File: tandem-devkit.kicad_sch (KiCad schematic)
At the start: 24 parts, among them J101 Conn_01x03, J102 Conn_01x03, J103 Conn_01x04, J104 Conn_01x02, J105 QWIIC I2C Connector

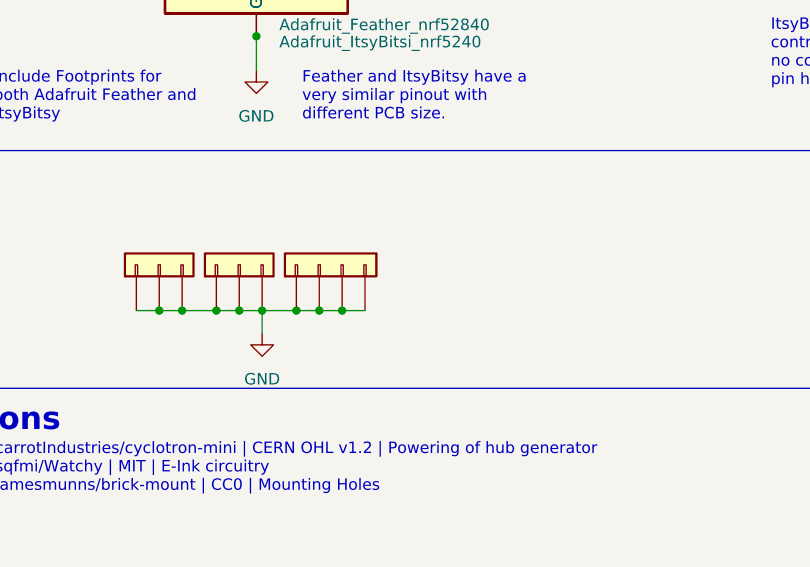
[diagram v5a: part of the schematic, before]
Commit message: prepare for touch button routing
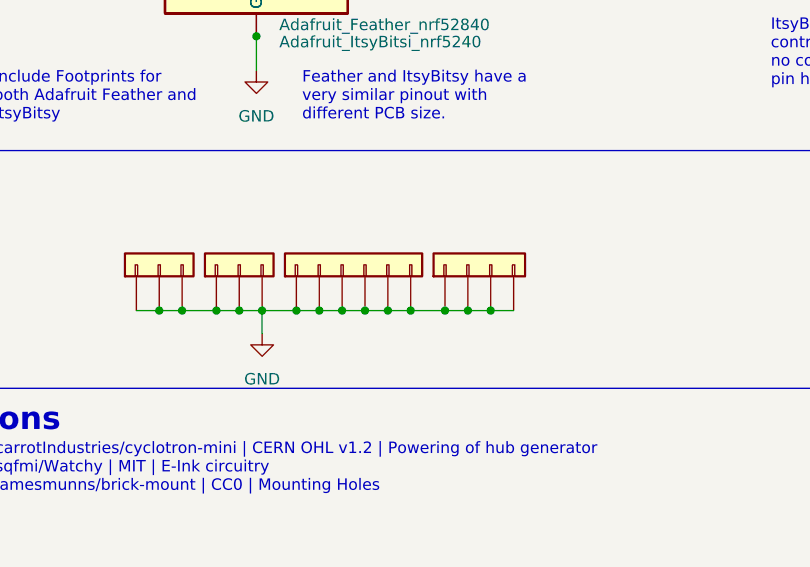
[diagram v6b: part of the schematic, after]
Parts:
- added J?: Conn_01x04, project-lib:brick-2x2, symbol Connector_Generic:Conn_01x04
- J103: value Conn_01x04 -> Conn_01x06; footprint brick-mount:brick-1x4 -> brick-mount:brick-1x6; symbol Connector_Generic:Conn_01x04 -> Connector_Generic:Conn_01x06
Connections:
- net GND: now also J103.5 (Pin_5), J103.6 (Pin_6), J?.1 (Pin_1), J?.2 (Pin_2), J?.3 (Pin_3), J?.4 (Pin_4)
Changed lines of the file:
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@@
   (junction (at 207.645 138.43) (diameter 0) (color 0 0 0 0)
   )
+  (junction (at 73.025 157.48) (diameter 0) (color 0 0 0 0)
+  )
   (junction (at 73.66 96.52) (diameter 0) (color 0 0 0 0)
   )
   (junction (at 48.26 83.82) (diameter 0) (color 0 0 0 0)
   )
+  (junction (at 86.995 157.48) (diameter 0) (color 0 0 0 0)
+  )
   (junction (at 48.26 73.66) (diameter 0) (color 0 0 0 0)
   )
@@
   (junction (at 63.5 63.5) (diameter 0) (color 0 0 0 0)
   )
+  (junction (at 75.565 157.48) (diameter 0) (color 0 0 0 0)
+  )
   (junction (at 61.595 157.48) (diameter 0) (color 0 0 0 0)
   )
   (junction (at 48.26 99.06) (diameter 0) (color 0 0 0 0)
   )
+  (junction (at 84.455 157.48) (diameter 0) (color 0 0 0 0)
+  )
   (junction (at 60.96 127) (diameter 0) (color 0 0 0 0)
   )
@@
   (junction (at 56.515 157.48) (diameter 0) (color 0 0 0 0)
   )
+  (junction (at 78.105 157.48) (diameter 0) (color 0 0 0 0)
+  )
   (junction (at 70.485 157.48) (diameter 0) (color 0 0 0 0)
   )
@@
   )
   (junction (at 48.26 88.9) (diameter 0) (color 0 0 0 0)
+  )
+  (junction (at 81.915 157.48) (diameter 0) (color 0 0 0 0)
   )
   (junction (at 48.26 106.68) (diameter 0) (color 0 0 0 0)
@@
     (stroke (width 0) (type default) (color 0 0 0 0))
   )
+  (wire (pts (xy 86.995 157.48) (xy 89.535 157.48))
+    (stroke (width 0) (type default) (color 0 0 0 0))
+  )
   (polyline (pts (xy 163.195 139.7) (xy 163.195 35.56))
     (stroke (width 0) (type default) (color 0 0 0 0))
@@
     (stroke (width 0) (type default) (color 0 0 0 0))
   )
+  (wire (pts (xy 78.105 157.48) (xy 81.915 157.48))
+    (stroke (width 0) (type default) (color 0 0 0 0))
+  )
   (wire (pts (xy 60.96 127) (xy 60.96 130.81))
     (stroke (width 0) (type default) (color 0 0 0 0))
@@
   )
   (wire (pts (xy 56.515 157.48) (xy 59.055 157.48))
+    (stroke (width 0) (type default) (color 0 0 0 0))
+  )
+  (wire (pts (xy 75.565 157.48) (xy 78.105 157.48))
     (stroke (width 0) (type default) (color 0 0 0 0))
   )
@@
     (stroke (width 0) (type default) (color 0 0 0 0))
   )
+  (wire (pts (xy 81.915 157.48) (xy 84.455 157.48))
+    (stroke (width 0) (type default) (color 0 0 0 0))
+  )
   (polyline (pts (xy 174.244 166.116) (xy 174.244 195.58))
     (stroke (width 0) (type solid) (color 221 0 0 1))
@@
     (stroke (width 0) (type solid) (color 221 0 0 1))
   )
+  (wire (pts (xy 84.455 157.48) (xy 86.995 157.48))
+    (stroke (width 0) (type default) (color 0 0 0 0))
+  )
   (wire (pts (xy 43.815 114.3) (xy 48.26 114.3))
     (stroke (width 0) (type default) (color 0 0 0 0))
@@
   )
   (wire (pts (xy 47.625 157.48) (xy 50.165 157.48))
+    (stroke (width 0) (type default) (color 0 0 0 0))
+  )
+  (wire (pts (xy 73.025 157.48) (xy 75.565 157.48))
     (stroke (width 0) (type default) (color 0 0 0 0))
   )
@@
     (pin "3")
   )
+  (symbol (lib_id "Connector_Generic:Conn_01x04") (at 84.455 152.4 90) (unit 1)
+    (in_bom yes) (on_board yes) (fields_autoplaced)
+    (property "Reference" "J?" (id 0) (at 85.725 146.05 90)
+      (effects (font (size 1.27 1.27)) hide)
+    )
+    (property "Value" "Conn_01x04" (id 1) (at 85.725 148.59 90)
+      (effects (font (size 1.27 1.27)) hide)
+    )
+    (property "Footprint" "project-lib:brick-2x2" (id 2) (at 84.455 152.4 0)
+      (effects (font (size 1.27 1.27)) hide)
+    )
+    (property "Datasheet" "~" (id 3) (at 84.455 152.4 0)
+      (effects (font (size 1.27 1.27)) hide)
+    )
+    (pin "1")
+    (pin "2")
+    (pin "3")
+    (pin "4")
+  )
   (symbol (lib_id "Device:R") (at 198.12 110.49 0) (unit 1)
     (in_bom yes) (on_board yes)
@@
     (pin "2")
   )
-  (symbol (lib_id "Connector_Generic:Conn_01x04") (at 67.945 152.4 90) (unit 1)
+  (symbol (lib_id "Connector_Generic:Conn_01x06") (at 70.485 152.4 90) (unit 1)
     (in_bom yes) (on_board yes) (fields_autoplaced)
-    (property "Reference" "J103" (id 0) (at 73.66 151.1299 90)
+    (property "Reference" "J103" (id 0) (at 76.2 151.1299 90)
       (effects (font (size 1.27 1.27)) (justify right) hide)
     )
-    (property "Value" "Conn_01x04" (id 1) (at 73.66 153.6699 90)
+    (property "Value" "Conn_01x06" (id 1) (at 76.2 153.6699 90)
       (effects (font (size 1.27 1.27)) (justify right) hide)
     )
-    (property "Footprint" "brick-mount:brick-1x4" (id 2) (at 67.945 152.4 0)
-      (effects (font (size 1.27 1.27)) hide)
-    )
-    (property "Datasheet" "~" (id 3) (at 67.945 152.4 0)
+    (property "Footprint" "brick-mount:brick-1x6" (id 2) (at 70.485 152.4 0)
+      (effects (font (size 1.27 1.27)) hide)
+    )
+    (property "Datasheet" "~" (id 3) (at 70.485 152.4 0)
       (effects (font (size 1.27 1.27)) hide)
     )
@@
     (pin "3")
     (pin "4")
+    (pin "5")
+    (pin "6")
   )
   (symbol (lib_id "Device:R") (at 40.005 86.36 90) (unit 1)
@@
     )
     (path "/e95b30be-c55c-4c78-9932-8a6370cf2f1d"
-      (reference "J103") (unit 1) (value "Conn_01x04") (footprint "brick-mount:brick-1x4")
+      (reference "J103") (unit 1) (value "Conn_01x06") (footprint "brick-mount:brick-1x6")
     )
     (path "/ec9c36e9-9c09-4abd-9e21-b989c784b09b"
@@
       (reference "J303") (unit 1) (value "FPC10(0.5MM)") (footprint "project-lib:jlcpcb-C11050_FFC_1x10-1MP_P0.50mm_Horizontal")
     )
+    (path "/d65d0648-9caf-48a8-a5f7-2e07080e3aea"
+      (reference "J?") (unit 1) (value "Conn_01x04") (footprint "project-lib:brick-2x2")
+    )
     (path "/d5fdcc1b-217f-4399-86f5-956578dadb93/7c178f84-7da2-4e79-b146-9dc5d286d2ba"

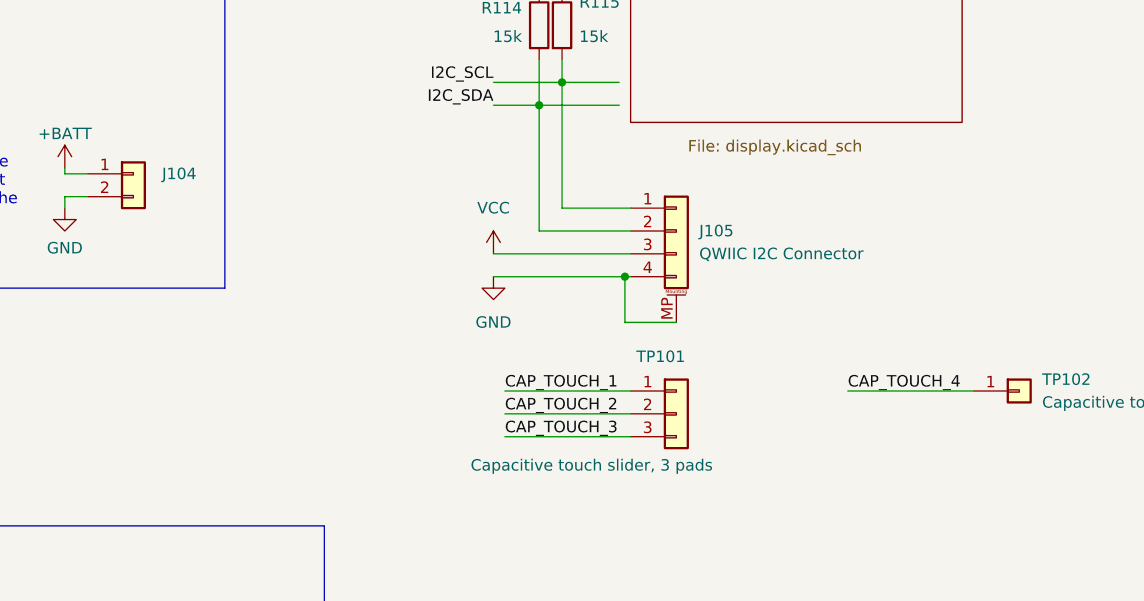
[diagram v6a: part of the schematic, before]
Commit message: PCB: route cap buttons and adjust zones
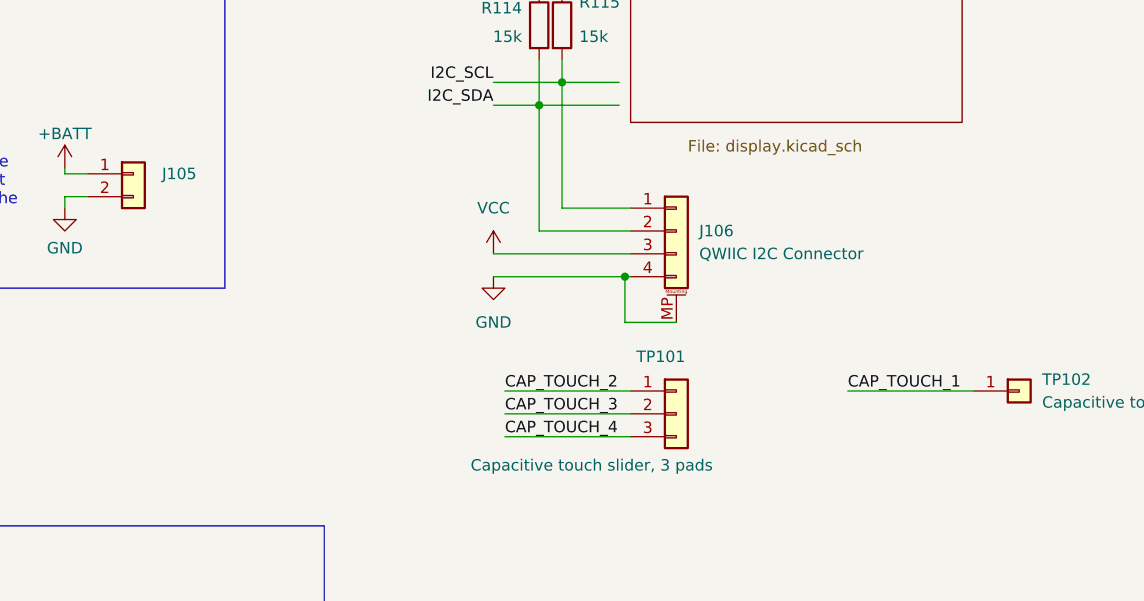
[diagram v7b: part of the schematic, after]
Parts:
- gave numbers to parts that had none: 1
- renumbered J104 to J105, J105 to J106
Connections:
- net CAP_TOUCH_1: now also TP102.1 (Pin_1); no longer TP101.1 (Pin_1)
- net CAP_TOUCH_2: now also TP101.1 (Pin_1); no longer TP101.2 (Pin_2)
- net CAP_TOUCH_3: now also TP101.2 (Pin_2); no longer TP101.3 (Pin_3)
- net CAP_TOUCH_4: now also TP101.3 (Pin_3); no longer TP102.1 (Pin_1)
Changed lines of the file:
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@@
     (effects (font (size 1.27 1.27)) (justify left bottom))
   )
-  (label "CAP_TOUCH_1" (at 194.31 151.13 0)
+  (label "CAP_TOUCH_1" (at 232.41 151.13 0)
     (effects (font (size 1.27 1.27)) (justify left bottom))
   )
@@
     (effects (font (size 1.27 1.27)) (justify left bottom))
   )
-  (label "CAP_TOUCH_4" (at 232.41 151.13 0)
+  (label "CAP_TOUCH_4" (at 194.31 156.21 0)
     (effects (font (size 1.27 1.27)) (justify left bottom))
   )
@@
     (effects (font (size 1.27 1.27)) (justify right bottom))
   )
-  (label "CAP_TOUCH_2" (at 194.31 153.67 0)
+  (label "CAP_TOUCH_2" (at 194.31 151.13 0)
     (effects (font (size 1.27 1.27)) (justify left bottom))
   )
@@
     (effects (font (size 1.27 1.27)) (justify left bottom))
   )
-  (label "CAP_TOUCH_3" (at 194.31 156.21 0)
+  (label "CAP_TOUCH_3" (at 194.31 153.67 0)
     (effects (font (size 1.27 1.27)) (justify left bottom))
   )
@@
   (symbol (lib_id "power:VCC") (at 193.04 135.89 0) (unit 1)
     (in_bom yes) (on_board yes) (fields_autoplaced)
-    (property "Reference" "#PWR0107" (id 0) (at 193.04 139.7 0)
+    (property "Reference" "#PWR0108" (id 0) (at 193.04 139.7 0)
       (effects (font (size 1.27 1.27)) hide)
     )
@@
   (symbol (lib_id "power:GND") (at 193.04 138.43 0) (unit 1)
     (in_bom yes) (on_board yes) (fields_autoplaced)
-    (property "Reference" "#PWR0108" (id 0) (at 193.04 144.78 0)
+    (property "Reference" "#PWR0109" (id 0) (at 193.04 144.78 0)
       (effects (font (size 1.27 1.27)) hide)
     )
@@
   (symbol (lib_id "power:VBUS") (at 63.5 57.15 0) (unit 1)
     (in_bom yes) (on_board yes)
-    (property "Reference" "#PWR0104" (id 0) (at 63.5 60.96 0)
+    (property "Reference" "#PWR0105" (id 0) (at 63.5 60.96 0)
       (effects (font (size 1.27 1.27)) hide)
     )
@@
   (symbol (lib_id "power:GND") (at 61.595 160.02 0) (unit 1)
     (in_bom yes) (on_board yes) (fields_autoplaced)
-    (property "Reference" "#PWR0110" (id 0) (at 61.595 166.37 0)
+    (property "Reference" "#PWR0104" (id 0) (at 61.595 166.37 0)
       (effects (font (size 1.27 1.27)) hide)
     )
@@
   (symbol (lib_id "power:VCC") (at 199.39 106.68 0) (unit 1)
     (in_bom yes) (on_board yes)
-    (property "Reference" "#PWR0109" (id 0) (at 199.39 110.49 0)
+    (property "Reference" "#PWR0110" (id 0) (at 199.39 110.49 0)
       (effects (font (size 1.27 1.27)) hide)
     )
@@
   (symbol (lib_id "power:+BATT") (at 145.415 126.365 0) (unit 1)
     (in_bom yes) (on_board yes)
-    (property "Reference" "#PWR0105" (id 0) (at 145.415 130.175 0)
+    (property "Reference" "#PWR0106" (id 0) (at 145.415 130.175 0)
       (effects (font (size 1.27 1.27)) hide)
     )
@@
   (symbol (lib_id "Connector_Generic_MountingPin:Conn_01x04_MountingPin") (at 213.36 133.35 0) (unit 1)
     (in_bom yes) (on_board yes) (fields_autoplaced)
-    (property "Reference" "J105" (id 0) (at 215.9 133.3499 0)
+    (property "Reference" "J106" (id 0) (at 215.9 133.3499 0)
       (effects (font (size 1.27 1.27)) (justify left))
     )
@@
   (symbol (lib_id "power:GND") (at 145.415 130.81 0) (unit 1)
     (in_bom yes) (on_board yes) (fields_autoplaced)
-    (property "Reference" "#PWR0106" (id 0) (at 145.415 137.16 0)
+    (property "Reference" "#PWR0107" (id 0) (at 145.415 137.16 0)
       (effects (font (size 1.27 1.27)) hide)
     )
@@
   (symbol (lib_id "Connector_Generic:Conn_01x04") (at 84.455 152.4 90) (unit 1)
     (in_bom yes) (on_board yes) (fields_autoplaced)
-    (property "Reference" "J?" (id 0) (at 85.725 146.05 90)
+    (property "Reference" "J104" (id 0) (at 85.725 146.05 90)
       (effects (font (size 1.27 1.27)) hide)
     )
@@
   (symbol (lib_id "Connector_Generic:Conn_01x02") (at 153.035 127 0) (unit 1)
     (in_bom yes) (on_board yes)
-    (property "Reference" "J104" (id 0) (at 156.21 126.9999 0)
+    (property "Reference" "J105" (id 0) (at 156.21 126.9999 0)
       (effects (font (size 1.27 1.27)) (justify left))
     )
@@
       (reference "#PWR0103") (unit 1) (value "GND") (footprint "")
     )
+    (path "/5609672f-1e6a-48cf-a156-8d669026c5a0"
+      (reference "#PWR0104") (unit 1) (value "GND") (footprint "")
+    )
     (path "/4cac86db-edbc-41fd-9ced-7a019bcc7397"
-      (reference "#PWR0104") (unit 1) (value "VBUS") (footprint "")
+      (reference "#PWR0105") (unit 1) (value "VBUS") (footprint "")
     )
     (path "/8ec9c310-02f6-40b9-a8d5-e4ecffebb930"
-      (reference "#PWR0105") (unit 1) (value "+BATT") (footprint "")
+      (reference "#PWR0106") (unit 1) (value "+BATT") (footprint "")
     )
     (path "/be8e8f37-585a-4fc0-9d9b-87158aac4d97"
-      (reference "#PWR0106") (unit 1) (value "GND") (footprint "")
+      (reference "#PWR0107") (unit 1) (value "GND") (footprint "")
     )
     (path "/1300bc03-ce1c-48a7-91f6-8f452e3f5b33"
-      (reference "#PWR0107") (unit 1) (value "VCC") (footprint "")
+      (reference "#PWR0108") (unit 1) (value "VCC") (footprint "")
     )
     (path "/25dcc88b-7d91-422f-a7ff-b87a4206a2e8"
-      (reference "#PWR0108") (unit 1) (value "GND") (footprint "")
+      (reference "#PWR0109") (unit 1) (value "GND") (footprint "")
     )
     (path "/5c2d26e7-d99d-408e-a6b5-fc989f467c55"
-      (reference "#PWR0109") (unit 1) (value "VCC") (footprint "")
-    )
-    (path "/5609672f-1e6a-48cf-a156-8d669026c5a0"
-      (reference "#PWR0110") (unit 1) (value "GND") (footprint "")
+      (reference "#PWR0110") (unit 1) (value "VCC") (footprint "")
     )
     (path "/d5fdcc1b-217f-4399-86f5-956578dadb93/fa0616dd-983c-46a3-85e8-1186c07f2350"
@@
       (reference "J103") (unit 1) (value "Conn_01x06") (footprint "brick-mount:brick-1x6")
     )
+    (path "/d65d0648-9caf-48a8-a5f7-2e07080e3aea"
+      (reference "J104") (unit 1) (value "Conn_01x04") (footprint "project-lib:brick-2x2")
+    )
     (path "/ec9c36e9-9c09-4abd-9e21-b989c784b09b"
-      (reference "J104") (unit 1) (value "Conn_01x02") (footprint "Connector_JST:JST_PH_B2B-PH-K_1x02_P2.00mm_Vertical")
+      (reference "J105") (unit 1) (value "Conn_01x02") (footprint "Connector_JST:JST_PH_B2B-PH-K_1x02_P2.00mm_Vertical")
     )
     (path "/acf09e5c-45d7-48f0-b893-8cae534e4cd2"
-      (reference "J105") (unit 1) (value "QWIIC I2C Connector") (footprint "project-lib:JST_SHL_SM04B-SHLS-TF_1x04-1MP_P1.00mm_Horizontal")
+      (reference "J106") (unit 1) (value "QWIIC I2C Connector") (footprint "project-lib:JST_SHL_SM04B-SHLS-TF_1x04-1MP_P1.00mm_Horizontal")
     )
     (path "/d5fdcc1b-217f-4399-86f5-956578dadb93/07c12313-4548-4085-a89a-89276ed43356"
@@
       (reference "J303") (unit 1) (value "FPC10(0.5MM)") (footprint "project-lib:jlcpcb-C11050_FFC_1x10-1MP_P0.50mm_Horizontal")
     )
-    (path "/d65d0648-9caf-48a8-a5f7-2e07080e3aea"
-      (reference "J?") (unit 1) (value "Conn_01x04") (footprint "project-lib:brick-2x2")
-    )
     (path "/d5fdcc1b-217f-4399-86f5-956578dadb93/7c178f84-7da2-4e79-b146-9dc5d286d2ba"

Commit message: PCB: Touchbuttons and silkscreen adaptions
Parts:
- TP102: footprint (none) -> project-lib:CapBtn_Board_edge
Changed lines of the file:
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@@
       (effects (font (size 1.27 1.27)) (justify left))
     )
-    (property "Footprint" "" (id 2) (at 251.46 151.13 0)
+    (property "Footprint" "project-lib:CapBtn_Board_edge" (id 2) (at 251.46 151.13 0)
       (effects (font (size 1.27 1.27)) hide)
     )
@@
     )
     (path "/3e0342fa-a68d-42cd-a22b-ccf1317d123e"
-      (reference "TP102") (unit 1) (value "Capacitive touch button") (footprint "")
+      (reference "TP102") (unit 1) (value "Capacitive touch button") (footprint "project-lib:CapBtn_Board_edge")
     )
     (path "/d5fdcc1b-217f-4399-86f5-956578dadb93/c53873f5-9695-4025-af4f-ae2b36f12765"
